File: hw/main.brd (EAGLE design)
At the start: 39.4 x 49.7 mm, 40 parts, among them Q1 732-MC14632.76KA-A0R, T1 863-MMBT4401LT1G, T2 863-MMBT4401LT1G, T3 863-MMBT4401LT1G, U1 579-MCP1703T-3002ECB, U2 638-CLS1522CL213RTR8, U3 595-MSP430G2553IPW28, U4 638-CLS1522CL213RTR8, X1 798-DF134P125H51, X2 798-DF134P125H51

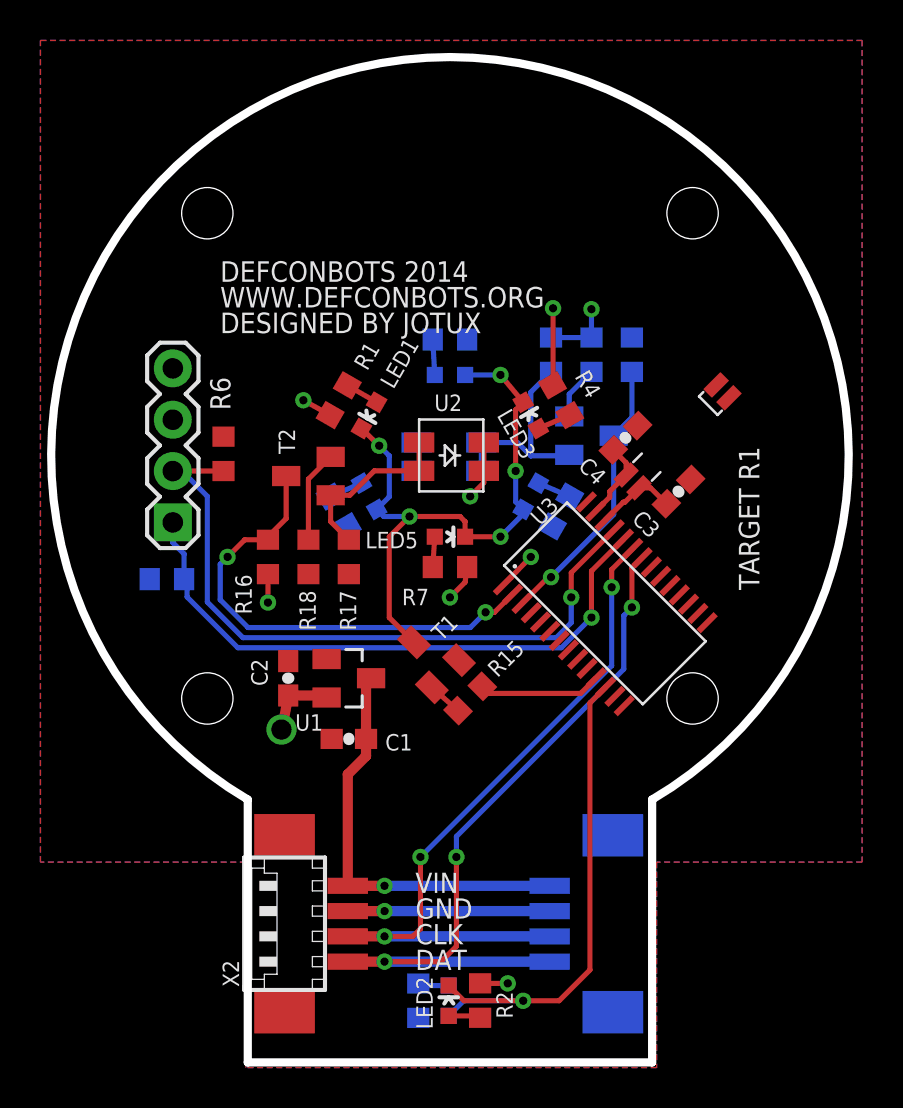
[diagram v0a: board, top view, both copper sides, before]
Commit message: Remove transistor and switch laser input to ADC polling.
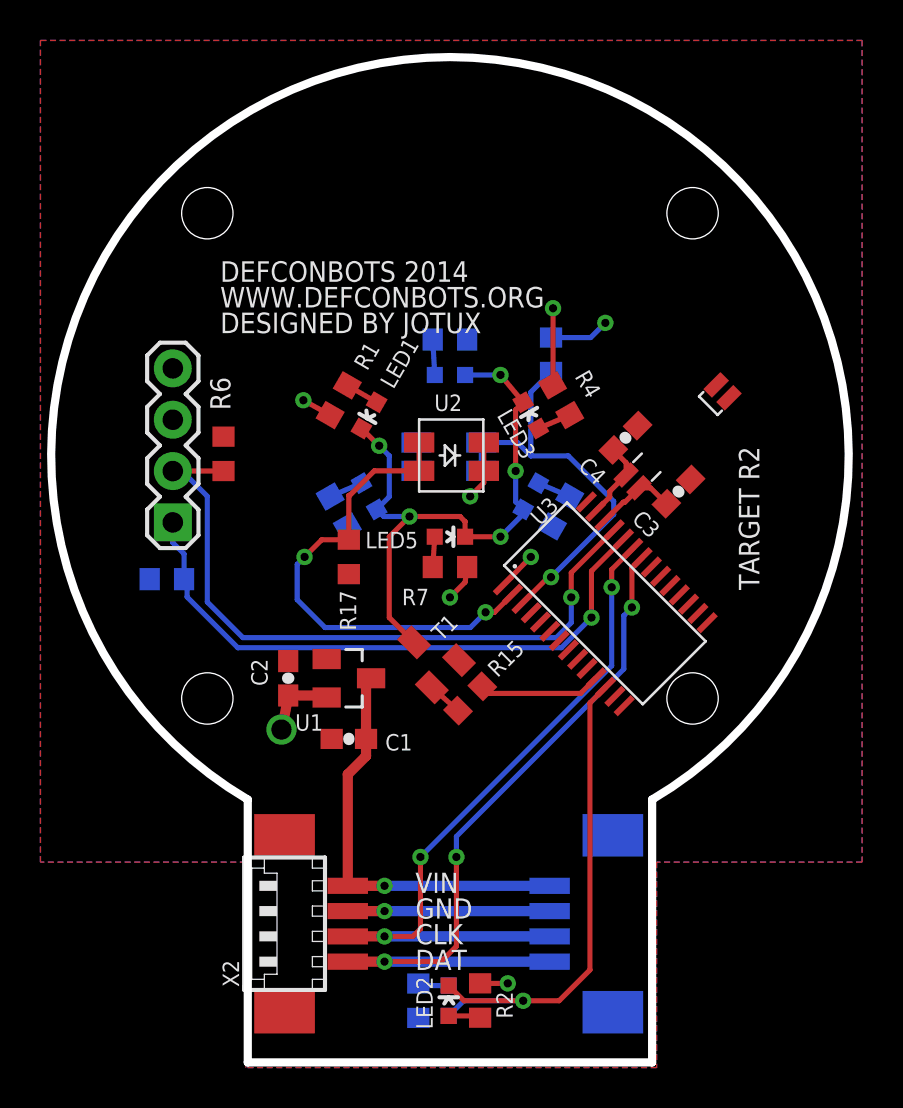
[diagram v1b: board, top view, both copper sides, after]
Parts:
- removed R16, R19: 667-ERJ-3EKF1002V, rcl:R0603
- removed R18, R21: 71-CRCW0603-390-E3, rcl:R0603
- removed T2, T3: 863-MMBT4401LT1G, transistor:SOT23-BEC
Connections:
- removed net 1: R20.2, T3.B, U4.1, U4.2
- removed net 121231: R17.2, T2.B, U2.1, U2.2
- removed net LED2: U3.13
- removed net LED3: U3.14
- removed net N$2: R18.2, T2.E
- removed net N$3: R21.2, T3.E
- net +3V3: no longer R16.2, R19.2
- net GND: no longer R18.1, R21.1
- net PEW_PEW_1: now also R17.2, U2.1, U2.2; no longer R16.1, T2.C
- net PEW_PEW_2: now also R20.2, U4.1, U4.2; no longer R19.1, T3.C
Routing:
- net 1: track 10.6 -> 0.00 mm
- net 121231: track 8.85 -> 0.00 mm
- net PEW_PEW_2: track 13.8 -> 20.7 mm
- net N$2: track 4.56 -> 0.00 mm
- net N$3: track 2.66 -> 0.00 mm
- net +3V3: track 18.5 -> 17.1 mm, vias 8 -> 7
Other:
- board text added: "TARGET R2"
- board text removed: "TARGET R1"

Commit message: Fix resistor value for light detector.
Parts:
- R17, R20: value 660-RK73H1JTTD4702F -> 71-CRCW06035M90FKEA
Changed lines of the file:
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@@
 </element>
 <element name="Q1" library="SparkFun" package="CRYSTAL-32KHZ-SMD_EPSON_MC146" value="732-MC14632.76KA-A0R" x="29.391690625" y="28.034678125" smashed="yes" rot="R45"/>
-<element name="R17" library="rcl" package="R0603" value="660-RK73H1JTTD4702F" x="15.254" y="25.254" smashed="yes" rot="R90">
+<element name="R17" library="rcl" package="R0603" value="71-CRCW06035M90FKEA" x="15.254" y="25.254" smashed="yes" rot="R90">
 <attribute name="NAME" x="15.619" y="21.619" size="0.8128" layer="25" font="vector" rot="R90"/>
 <attribute name="VALUE" x="17.159" y="24.619" size="0.8128" layer="27" font="vector" rot="R90"/>
@@
 <attribute name="VALUE" x="21.805" y="24.432" size="0.8128" layer="28" font="vector" rot="MR0"/>
 </element>
-<element name="R20" library="rcl" package="R0603" value="660-RK73H1JTTD4702F" x="25.254" y="35.254" smashed="yes" rot="MR270">
+<element name="R20" library="rcl" package="R0603" value="71-CRCW06035M90FKEA" x="25.254" y="35.254" smashed="yes" rot="MR270">
 <attribute name="NAME" x="24.619" y="36.389" size="0.8128" layer="26" font="vector" rot="MR270"/>
 <attribute name="VALUE" x="27.159" y="35.889" size="0.8128" layer="28" font="vector" rot="MR270"/>

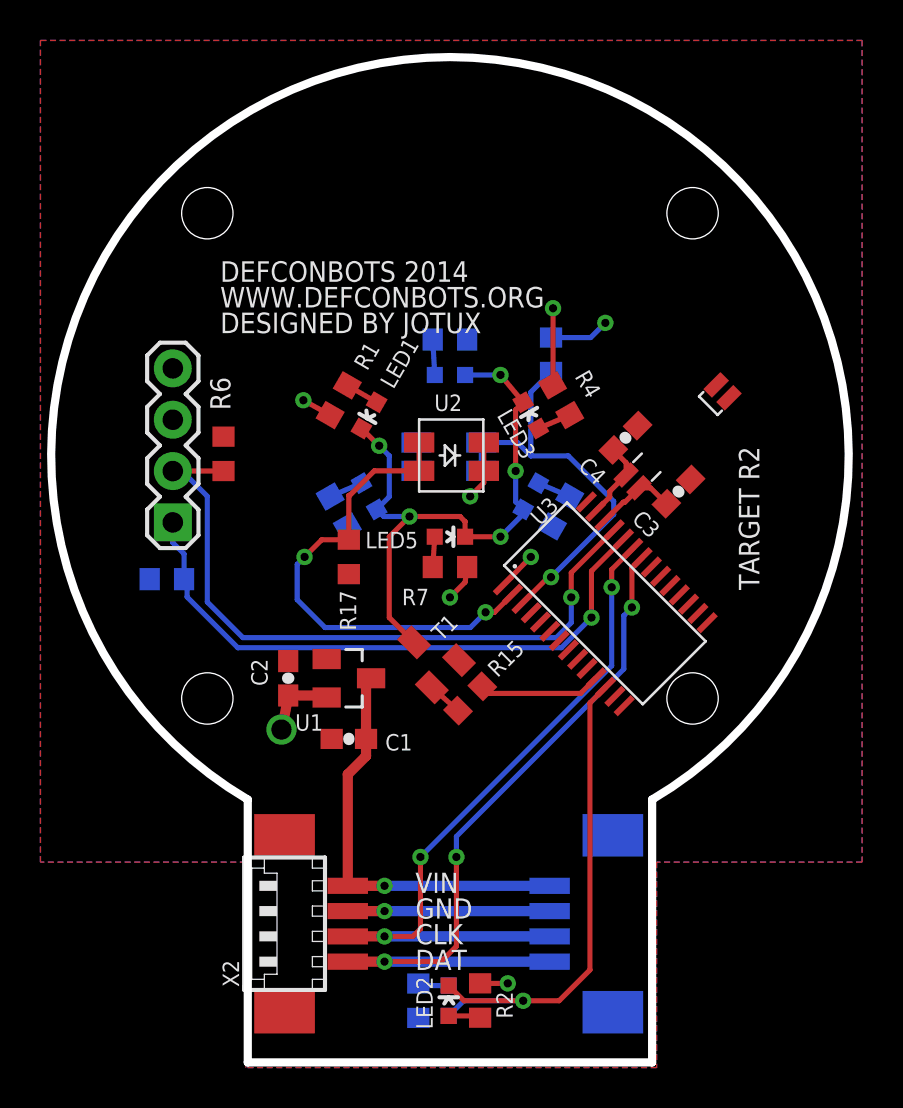
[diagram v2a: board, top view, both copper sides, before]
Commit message: Updated target to simplify circuit and make immune to spurious light sources.
The design has been reduced in size from ~40mm diameter to ~21mm diameter. The sensor was changed from a single-color (red) detector to a full-spectrum + white sensor since the old version would get tripped by white light (and camera flashes). The microcontroller was changed from the MSP430G2553 to the MSP430G2452 in the 14 pin package to save space. The new target will mount from the bottom and sit in the bottom of the table tennis ball instead of in the middle.
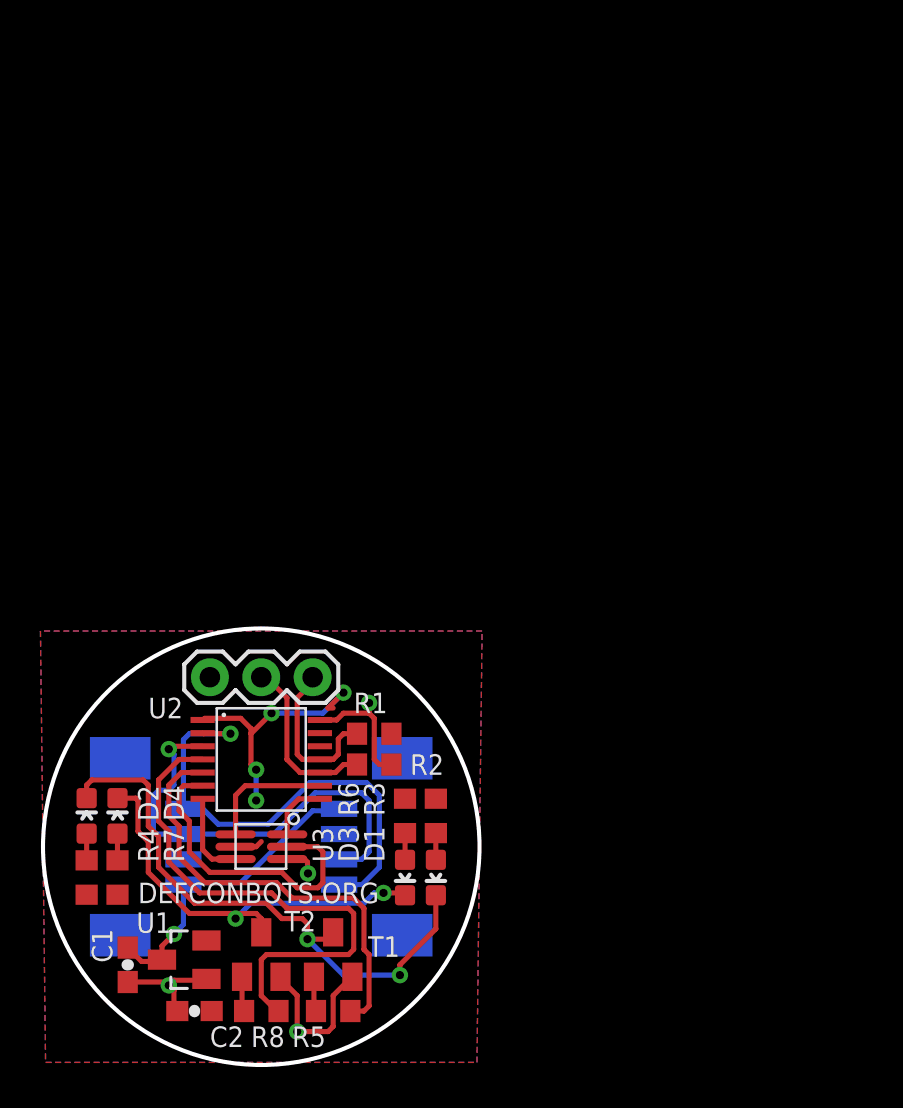
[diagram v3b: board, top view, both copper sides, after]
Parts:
- removed C3, C4: 80-C0603C180J4G, SparkFun-Passives:0603-CAP
- removed LED1, LED11, LED3, LED5, LED7, LED9: 78-VLMB1300-GS08, SparkFun-LED:LED-0603
- removed LED2, LED4: 720-LGQ971-KN-1, SparkFun-LED:LED-0603
- removed Q1: 732-MC14632.76KA-A0R, SparkFun:CRYSTAL-32KHZ-SMD_EPSON_MC146
- removed R11, R13, R15, R9: 71-CRCW0603-390-E3, rcl:R0603
- removed R17, R20: 71-CRCW06035M90FKEA, rcl:R0603
- removed U4: 638-CLS1522CL213RTR8, torpedo:CLS15
- added D1, D2: VLMB1300-GS08, SparkFun-LED:LED-0603
- added D3, D4: VLMS1300-GS08, SparkFun-LED:LED-0603
- added R8: CRCW0603200RFKEA, rcl:R0603
- added T2: PMBT4401,215, transistor:SOT23-BEC
- C1, C2: value 810-C1608X5R1C106M -> C1608X5R1C106M080AB
- JP1: device SparkFun:1X04 -> SparkFun-Connectors:1X03
- R1, R2: value 71-CRCW0603-390-E3 -> RK73H1JTTD4702F
- R3, R6: value 660-RK73H1JTTD4702F -> CRCW0603200RFKEA
- R4, R5, R7: value 71-CRCW0603-390-E3 -> CRCW0603200RFKEA
- T1: value 863-MMBT4401LT1G -> PMBT4401,215
- U1: value 579-MCP1703T-3002ECB -> MCP1703T-3002E/CB
- U2: value 638-CLS1522CL213RTR8 -> MSP430G2452IPW14R; device torpedo:CLS15 -> TI_MSP430_v16:PW14
- U3: value 595-MSP430G2553IPW28 -> TCS3414CS; device torpedo:PW28 -> torpedo:CS-6
- X1, X2: value 798-DF134P125H51 -> DF13-4P-1.25V(50); device con-molex:53261-04 -> con-molex:53398-04
- moved R4 33.3 mm to (2.29, 9.40), turned to 270 degrees
- moved R7 22.5 mm to (3.81, 9.40), turned to 270 degrees
- moved U3 20.8 mm to (10.9, 10.9), turned to 270 degrees
- moved R6 20.0 mm to (18.0, 12.4), turned to 90 degrees
- moved R3 17.7 mm to (19.6, 12.4), flipped to the top, turned to 90 degrees
- moved C2 17.1 mm to (7.62, 2.79), turned to 180 degrees
- moved R1 16.6 mm to (16.5, 16.5), turned to 0 degrees
- moved U2 16.3 mm to (10.9, 15.2), turned to 270 degrees
- moved U1 16.1 mm to (7.11, 5.33), turned to 90 degrees
- moved C1 15.6 mm to (4.32, 5.08), turned to 270 degrees
- moved T1 15.4 mm to (14.5, 5.59), turned to 0 degrees
- moved R2 12.8 mm to (16.5, 15.0), turned to 180 degrees
- moved X1 11.1 mm to (17.3, 10.9)
- moved JP1 10.3 mm to (13.5, 19.3), turned to 180 degrees
- moved X2 8.98 mm to (4.57, 10.9), flipped to the bottom, turned to 270 degrees
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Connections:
- removed net EN_LED: R15.2, U3.11
- removed net LED1: LED2.C, LED4.C, U3.12
- removed net N$11: LED7.A, R9.1
- removed net N$12: C4.1, Q1.P$2, U3.27
- removed net N$13: C3.1, Q1.P$1, U3.26
- removed net N$5: LED1.A, R1.1
- removed net N$9: LED4.A, R5.1
- removed net PEW_PEW_1: R17.2, U2.1, U2.2, U3.2
- removed net PEW_PEW_2: R20.2, U3.3, U4.1, U4.2
- new net BLUE_LED: R5.2, U2.5
- new net CNT: U2.2, X1.4, X2.4
- new net INT: U2.7, U3.B3
- new net N$2: D3.C, D4.C, T2.C
- new net RED_LED: R8.2, U2.4
- new net SET: U2.3, X1.3, X2.3
- new net SYNC: U2.6, U3.A2
- net +3V3: now also R6.2, U2.1, U3.B2; no longer JP1.4, R11.2, R13.2, R2.2, R5.2, R9.2, U2.3, U2.4, U3.1, U4.3, U4.4
- net CLK: now also U2.8, U3.A1; no longer U3.23, X1.3, X2.3
- net DAT: now also U2.9, U3.B1; no longer U3.22, X1.4, X2.4
- net GND: now also R2.1, T2.E, U2.14, U3.A3; no longer C3.2, C4.2, R17.1, R20.1, R6.1, U3.28
- net LED: now also D1.C, D2.C; no longer LED1.C, LED11.C, LED3.C, LED5.C, LED7.C, LED9.C
- net N$1: now also D4.A; no longer LED5.A
- net N$10: now also D3.A, R6.1; no longer LED2.A, R2.1
- net N$18: now also R5.1; no longer R15.1
- net N$4: now also R8.1, T2.B; no longer LED3.A, R4.1
- net N$6: now also D2.A, R4.1; no longer LED11.A, R13.1
- net N$7: now also D1.A, R3.1; no longer LED9.A, R11.1
- net RST: now also JP1.2, R2.2, U2.10; no longer JP1.1, R3.1, U3.24
- net TEST: now also JP1.1, R1.1, U2.11; no longer JP1.2, R6.2, U3.25
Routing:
- net CLK: track 35.1 -> 3.04 mm, vias 3 -> 0
- net DAT: track 36.9 -> 6.30 mm, vias 3 -> 0
- net RED_LED: track 0.00 -> 26.6 mm
- net TEST: track 34.5 -> 8.16 mm, vias 1 -> 0
- net LED1: track 26.2 -> 0.00 mm, vias 1 -> 0
- net PEW_PEW_1: track 24.3 -> 0.00 mm, vias 2 -> 0
- net CNT: track 0.00 -> 24.3 mm, vias 0 -> 1
- net SET: track 0.00 -> 22.5 mm, vias 0 -> 1
- net BLUE_LED: track 0.00 -> 21.9 mm
- net RST: track 30.4 -> 8.64 mm, vias 1 -> 0
- net N$2: track 0.00 -> 21.3 mm, vias 0 -> 2
- net PEW_PEW_2: track 20.7 -> 0.00 mm, vias 1 -> 0
- net SYNC: track 0.00 -> 15.4 mm
- net GND: track 13.0 -> 21.7 mm, vias 2 -> 4
- net EN_LED: track 6.11 -> 0.00 mm
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- added copper zone on layer 1, net +3V3
- added copper zone on layer 16, net GND
- removed copper zone on layer 16, net +3V3
- removed copper zone on layer 1, net GND
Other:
- board size 39.4 x 49.7 mm -> 21.6 x 21.6 mm
- board text added: "DEFCONBOTS.ORG"
- board text removed: "CLK"
- board text removed: "DAT"
- board text removed: "DEFCONBOTS 2014"
- board text removed: "DESIGNED BY JOTUX"
- board text removed: "GND"
- board text removed: "RST"
- board text removed: "TARGET R2"
- board text removed: "TEST"
- board text removed: "VCC"
- board text removed: "VIN"
- board text removed: "WWW.DEFCONBOTS.ORG"

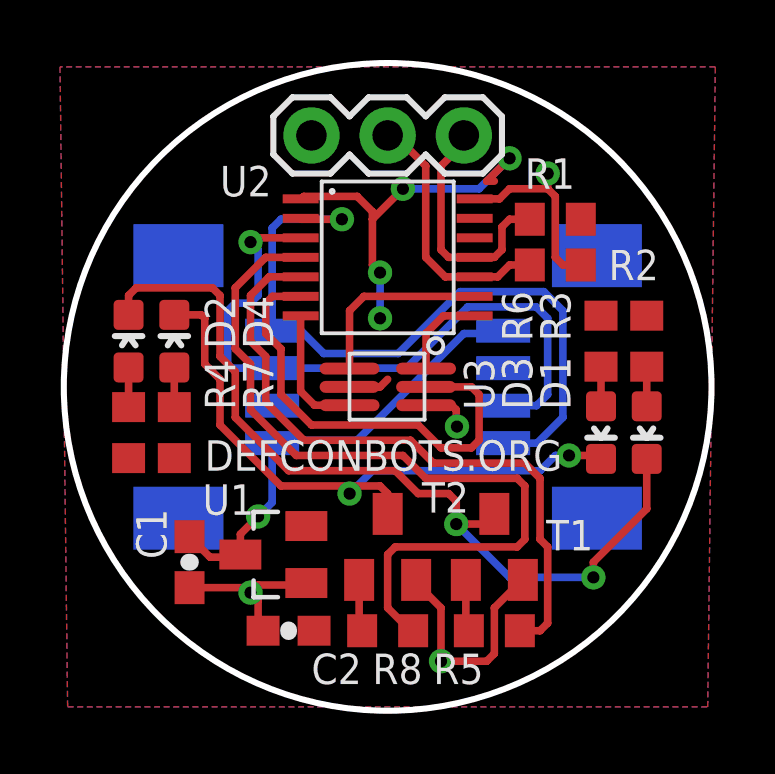
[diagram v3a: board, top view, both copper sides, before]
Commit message: Fix errors in PCB found after initial testing.
 - Swapped pullup/down on RST/TEST lines (they were backward).
 - Added 4.7k pullups to i2c lines (maybe don't need but the signal is a little ugly without them)
 - Removed silkscreen of part numbers since they're not very readable anyway
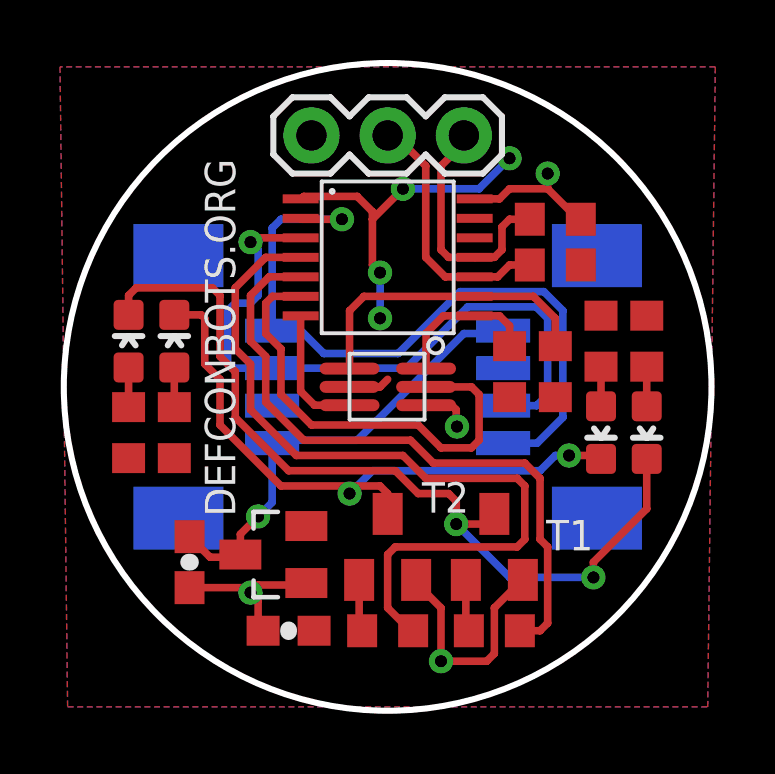
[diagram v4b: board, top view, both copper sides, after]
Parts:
- added R10, R9: RK73H1JTTD4701F, rcl:R0603
- moved R1 1.52 mm to (16.5, 15.0)
- moved R2 1.52 mm to (16.5, 16.5)
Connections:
- net +3V3: now also R10.2, R9.2
- net CLK: now also R10.1
- net DAT: now also R9.1
- net RST: now also R1.1; no longer R2.2
- net TEST: now also R2.2; no longer R1.1
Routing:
- net DAT: track 6.30 -> 10.2 mm
- net CLK: track 3.04 -> 5.02 mm
- net GND: track 21.7 -> 19.9 mm
- net +3V3: track 14.4 -> 13.1 mm
